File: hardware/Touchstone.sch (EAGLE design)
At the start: 69 parts, among them J3 USB-MICROB, U1 NEOPIXEL_NANO_2427, U10 TSL2591, U11 915MHz, U12 MH-Z19, U13 CCS811-I2C, U14 IAQ-CORE-C, U15 VLP-450-F, U16 VLP-450-F, U2 FT231XQ-R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

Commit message: Added pullups on CCS811's signal lines
RESET AND WAKE lines pulled up by default
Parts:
- added R12, R14: 100K, Adafruit Feather 32u4 Bluefruit LE:MICROBUILDER_RESISTOR_0402MP
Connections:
- new net N$6: R12.2, U13.RESET
- net D5: now also R14.2
- net VCC: now also R12.1, R14.1
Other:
- note added: "0.57"
- note removed: "0.56b"
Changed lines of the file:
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@@
 <?xml version="1.0" encoding="utf-8"?>
 <!DOCTYPE eagle SYSTEM "eagle.dtd">
-<eagle version="8.2.2">
+<eagle version="8.3.0">
 <drawing>
 <settings>
 <setting alwaysvectorfont="no"/>
+<setting keepoldvectorfont="yes"/>
 <setting verticaltext="up"/>
 </settings>
@@
 <part name="U$4" library="0878980426" deviceset="0878980426" device=""/>
 <part name="U$5" library="0878980426" deviceset="0878980426" device=""/>
+<part name="R12" library="Adafruit Feather 32u4 Bluefruit LE" deviceset="MICROBUILDER_RESISTOR" device="_0402MP" value="100K"/>
+<part name="R14" library="Adafruit Feather 32u4 Bluefruit LE" deviceset="MICROBUILDER_RESISTOR" device="_0402MP" value="100K"/>
+<part name="SUPPLY19" library="SparkFun-Aesthetics" deviceset="VCC" device=""/>
+<part name="SUPPLY20" library="SparkFun-Aesthetics" deviceset="VCC" device=""/>
 </parts>
 <sheets>
@@
 <text x="88.9" y="55.88" size="1.778" layer="97">0x5A</text>
 <text x="220.98" y="104.14" size="1.778" layer="97">0x77</text>
-<text x="257.556" y="-102.362" size="2.54" layer="94" font="vector" ratio="10">0.56b</text>
+<text x="257.556" y="-102.362" size="2.54" layer="94" font="vector" ratio="10">0.57</text>
 <text x="248.666" y="-87.122" size="2.54" layer="94" font="vector" ratio="10">github.crtlabs.org</text>
 <text x="157.48" y="101.6" size="1.778" layer="97">0x29</text>
@@
 <instance part="U$4" gate="G$1" x="259.08" y="101.6"/>
 <instance part="U$5" gate="G$1" x="289.56" y="101.6"/>
+<instance part="R12" gate="G$1" x="58.42" y="20.32" rot="R270"/>
+<instance part="R14" gate="G$1" x="109.22" y="20.32" rot="R270"/>
+<instance part="SUPPLY19" gate="G$1" x="58.42" y="25.4"/>
+<instance part="SUPPLY20" gate="G$1" x="109.22" y="25.4"/>
 </instances>
 <busses>
@@
 <pinref part="SUPPLY18" gate="G$1" pin="VCC"/>
 </segment>
+<segment>
+<pinref part="R12" gate="G$1" pin="1"/>
+<pinref part="SUPPLY19" gate="G$1" pin="VCC"/>
+</segment>
+<segment>
+<pinref part="R14" gate="G$1" pin="1"/>
+<pinref part="SUPPLY20" gate="G$1" pin="VCC"/>
+</segment>
 </net>
 <net name="SCL" class="0">
@@
 <wire x1="101.6" y1="7.62" x2="106.68" y2="7.62" width="0.1524" layer="91"/>
 <label x="101.6" y="7.62" size="1.778" layer="95"/>
+<wire x1="106.68" y1="7.62" x2="109.22" y2="7.62" width="0.1524" layer="91"/>
+<wire x1="106.68" y1="7.62" x2="106.68" y2="12.7" width="0.1524" layer="91"/>
+<junction x="106.68" y="7.62"/>
+<pinref part="R14" gate="G$1" pin="2"/>
+<wire x1="106.68" y1="12.7" x2="109.22" y2="12.7" width="0.1524" layer="91"/>
+<wire x1="109.22" y1="12.7" x2="109.22" y2="15.24" width="0.1524" layer="91"/>
 </segment>
 </net>
@@
 <wire x1="269.24" y1="55.88" x2="269.24" y2="63.5" width="0.1524" layer="91"/>
 <label x="261.62" y="55.88" size="1.778" layer="95"/>
+</segment>
+</net>
+<net name="N$6" class="0">
+<segment>
+<pinref part="U13" gate="G$1" pin="RESET"/>
+<pinref part="R12" gate="G$1" pin="2"/>
+<wire x1="66.04" y1="12.7" x2="58.42" y2="12.7" width="0.1524" layer="91"/>
+<wire x1="58.42" y1="12.7" x2="58.42" y2="15.24" width="0.1524" layer="91"/>
 </segment>
 </net>
@@
 </note>
 <note version="8.2" severity="warning">
-Since Version 8.2, Eagle supports online libraries. The ids
+Since Version 8.2, EAGLE supports online libraries. The ids
 of those online libraries will not be understood (or retained)
 with this version.

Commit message: Added SMD pads for T/RH breakout
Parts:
- added U$6: CONN_HDR_1.27MM_SMD_4POS, CONN_HDR_1.27MM_SMD_4POS:CONN_HDR_1.27MM_SMD_4POS
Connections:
- net GND: now also U$6.P$4
- net SCL: now also U$6.P$2
- net SDA: now also U$6.P$3
- net VCC: now also U$6.P$1
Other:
- note added: "T/RH Headers"
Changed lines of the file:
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@@
 <part name="SUPPLY1" library="SparkFun-Aesthetics" deviceset="VCC" device=""/>
 <part name="SUPPLY7" library="SparkFun-Aesthetics" deviceset="VCC" device=""/>
-<part name="U8" library="linear" library_urn="urn:adsk.eagle:library:262" deviceset="MCP1703" device="CB">
+<part name="U8" library="linear" library_urn="urn:adsk.eagle:library:262" deviceset="MCP1703" device="CB" package3d_urn="urn:adsk.eagle:package:16489/1">
 <attribute name="MF" value=""/>
 <attribute name="MPN" value="MCP1703T-2502E/CB"/>
@@
 <part name="SUPPLY19" library="SparkFun-Aesthetics" deviceset="VCC" device=""/>
 <part name="SUPPLY20" library="SparkFun-Aesthetics" deviceset="VCC" device=""/>
+<part name="U$6" library="CONN_HDR_1.27MM_SMD_4POS" deviceset="CONN_HDR_1.27MM_SMD_4POS" device=""/>
 </parts>
 <sheets>
@@
 <text x="157.48" y="101.6" size="1.778" layer="97">0x29</text>
 <text x="139.7" y="78.74" size="2.54" layer="94" font="vector">RGB LED</text>
-<text x="127" y="30.48" size="2.54" layer="94" font="vector">I2C Headers</text>
+<text x="124.46" y="30.48" size="2.54" layer="94" font="vector">I2C Headers</text>
 <text x="73.66" y="129.54" size="2.54" layer="94" font="vector">PM2.5 sensor</text>
 <text x="185.42" y="81.28" size="2.54" layer="94" font="vector">RFM69HCW</text>
@@
 <wire x1="180.34" y1="43.18" x2="180.34" y2="-12.7" width="0.1524" layer="94" style="longdash"/>
 <wire x1="116.84" y1="43.18" x2="180.34" y2="43.18" width="0.1524" layer="94" style="longdash"/>
-<text x="127" y="-5.08" size="2.54" layer="94" font="vector">5V Power</text>
+<text x="124.46" y="-5.08" size="2.54" layer="94" font="vector">5V Power</text>
 <wire x1="180.34" y1="43.18" x2="312.42" y2="43.18" width="0.1524" layer="94" style="longdash"/>
 <text x="91.44" y="-2.54" size="1.778" layer="97">0x5B</text>
 <text x="30.48" y="104.14" size="1.778" layer="97">0x40</text>
+<text x="124.46" y="12.7" size="2.54" layer="94" font="vector">T/RH Headers</text>
 </plain>
 <instances>
@@
 <instance part="SUPPLY19" gate="G$1" x="58.42" y="25.4"/>
 <instance part="SUPPLY20" gate="G$1" x="109.22" y="25.4"/>
+<instance part="U$6" gate="G$1" x="157.48" y="10.16"/>
 </instances>
 <busses>
@@
 <label x="274.32" y="99.06" size="1.778" layer="95"/>
 </segment>
+<segment>
+<pinref part="U$6" gate="G$1" pin="P$4"/>
+<wire x1="167.64" y1="10.16" x2="170.18" y2="10.16" width="0.1524" layer="91"/>
+<label x="170.18" y="10.16" size="1.778" layer="95"/>
+</segment>
 </net>
 <net name="VCC" class="0">
@@
 <pinref part="SUPPLY20" gate="G$1" pin="VCC"/>
 </segment>
+<segment>
+<pinref part="U$6" gate="G$1" pin="P$1"/>
+<wire x1="167.64" y1="17.78" x2="170.18" y2="17.78" width="0.1524" layer="91"/>
+<label x="170.18" y="17.78" size="1.778" layer="95"/>
+</segment>
 </net>
 <net name="SCL" class="0">
@@
 <label x="101.6" y="15.24" size="1.778" layer="95"/>
 </segment>
+<segment>
+<pinref part="U$6" gate="G$1" pin="P$2"/>
+<wire x1="167.64" y1="15.24" x2="170.18" y2="15.24" width="0.1524" layer="91"/>
+<label x="170.18" y="15.24" size="1.778" layer="95"/>
+</segment>
 </net>
 <net name="SDA" class="0">
@@
 <wire x1="101.6" y1="12.7" x2="104.14" y2="12.7" width="0.1524" layer="91"/>
 <label x="101.6" y="12.7" size="1.778" layer="95"/>
+</segment>
+<segment>
+<pinref part="U$6" gate="G$1" pin="P$3"/>
+<wire x1="167.64" y1="12.7" x2="170.18" y2="12.7" width="0.1524" layer="91"/>
+<label x="170.18" y="12.7" size="1.778" layer="95"/>
 </segment>
 </net>
@@
 with this version.
 </note>
+<note version="8.3" severity="warning">
+Since Version 8.3, EAGLE supports URNs for individual library
+assets (packages, symbols, and devices). The URNs of those assets
+will not be understood (or retained) with this version.
+</note>
+<note version="8.3" severity="warning">
+Since Version 8.3, EAGLE supports the association of 3D packages
+with devices in libraries, schematics, and board files. Those 3D
+packages will not be understood (or retained) with this version.
+</note>
 </compatibility>

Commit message: Version number change; minor adjustments
- Changed version number to 0.5.7 (new versioning format)
- silkscreen adjustments
- some schematic rearrangements
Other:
- note added: "0.5.7"
- note removed: "0.57"
- moved on the sheet: C18, C2, C3, J1, J2, JP1, R12, R14, R4, R7, R9, U1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

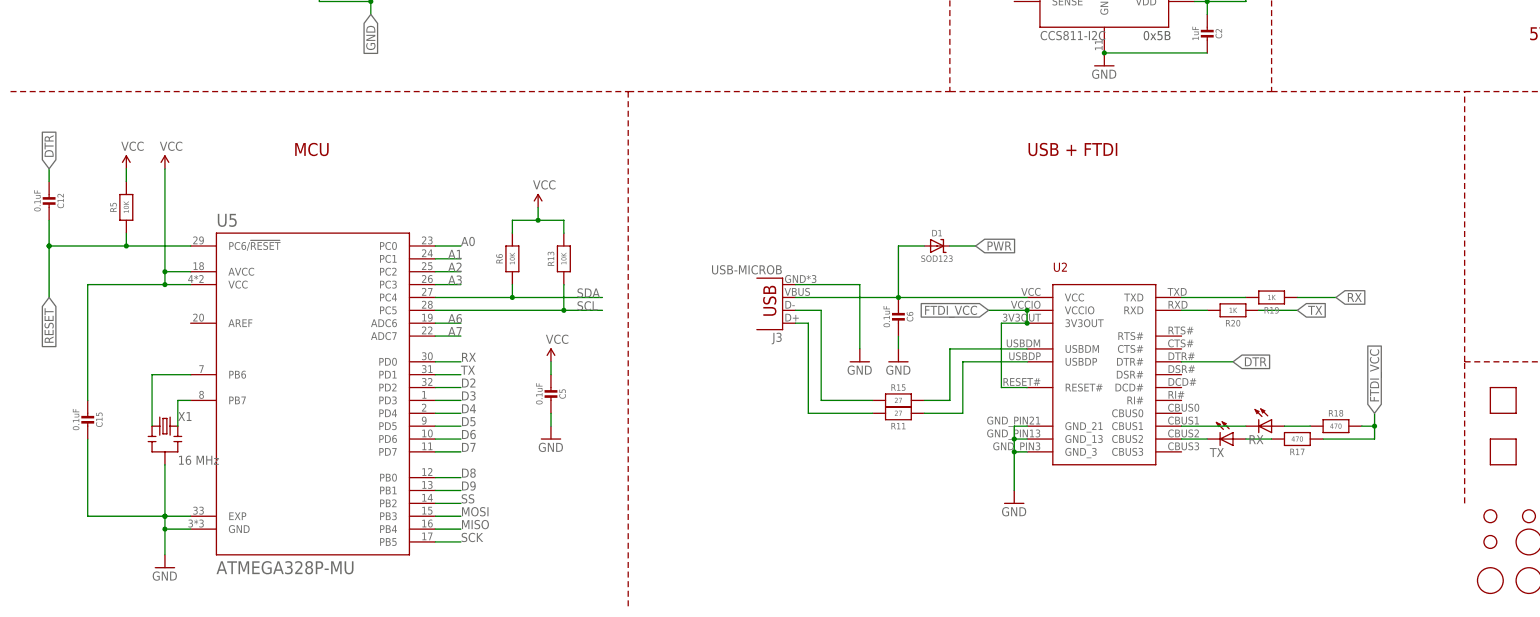
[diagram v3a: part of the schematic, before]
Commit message: Added reset button
- added momentary tactile button for resetting device (reconfiguring,
not power cycle)
- added other circuitry for button
- moved I2C headers to make space for reset button
- several traces redone to accomodate button
- minor silkscreen adjustment
- DRC/ERC checked
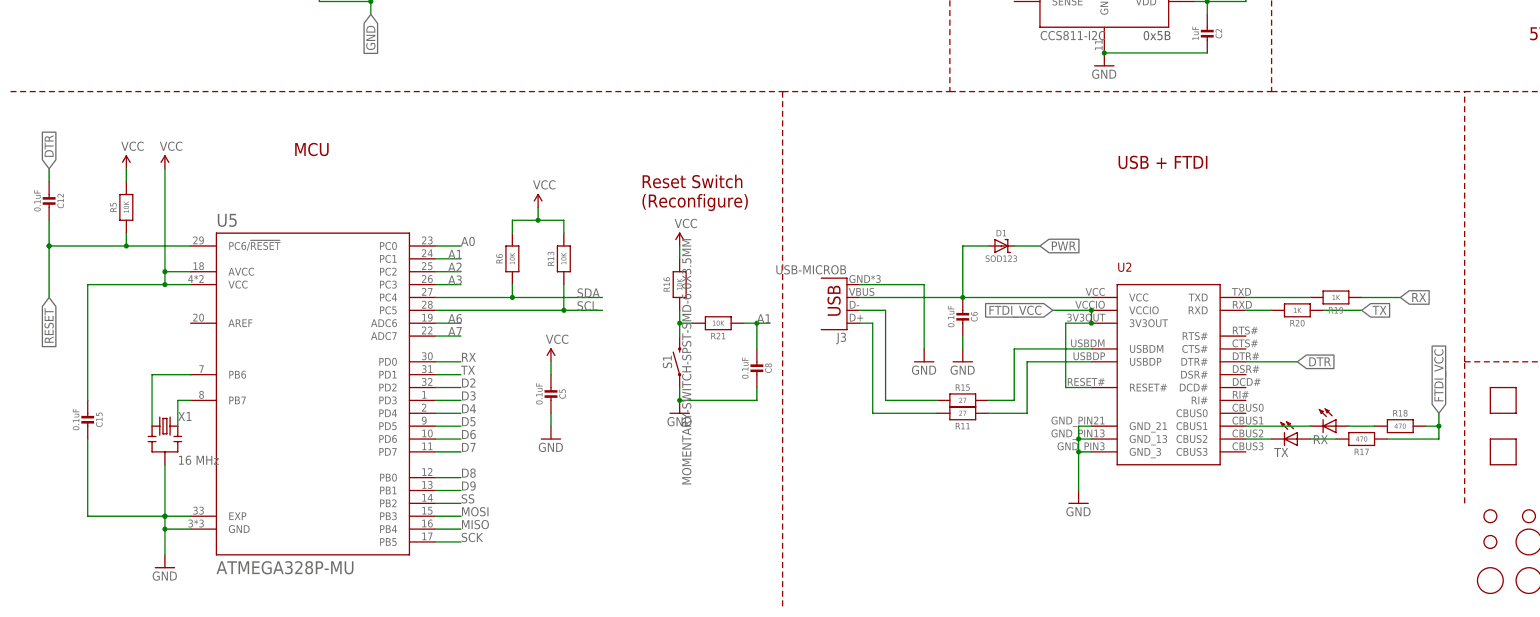
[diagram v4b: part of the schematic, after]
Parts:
- added C8: 0.1uF, Adafruit Feather 32u4 Bluefruit LE:MICROBUILDER_CAP_CERAMIC_0402MP
- added R16, R21: 10K, Adafruit Feather 32u4 Bluefruit LE:MICROBUILDER_RESISTOR_0402MP
- added S1: MOMENTARY-SWITCH-SPST-SMD-6.0X3.5MM, SparkFun-Switches:MOMENTARY-SWITCH-SPST-SMD-6.0X3.5MM
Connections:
- new net N$7: R16.1, R21.2, S1.2
- net A1: now also C8.2, R21.1
- net GND: now also C8.1, S1.1
- net VCC: now also R16.2
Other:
- note added: "Reset Switch (Reconfigure)"
- moved on the sheet: C6, D1, J3, R11, R15, R17, R18, R19, R20, RX, TX, U2

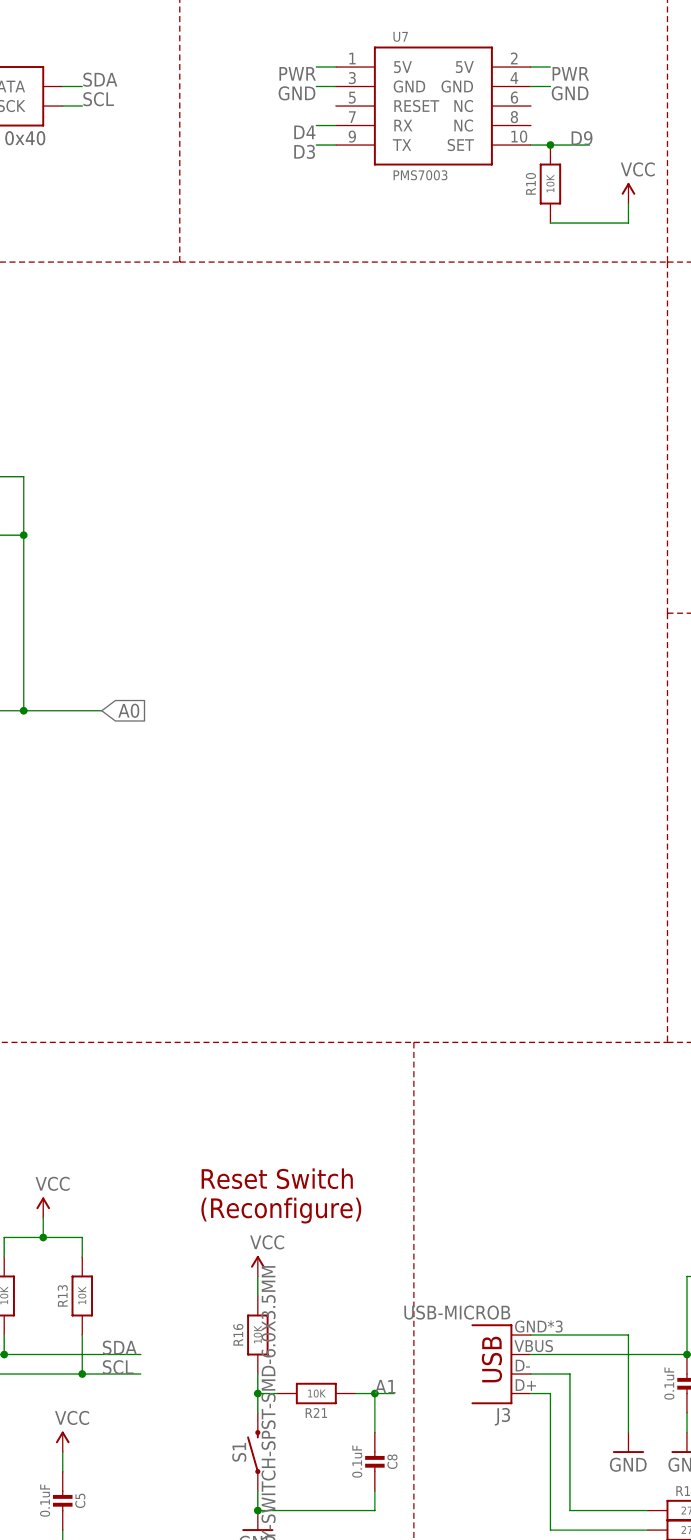
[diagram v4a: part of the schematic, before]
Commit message: Several routing adjustments
- PMS7003 TX rewired from D3 to A1 (D3 is INT pin)
- Button reqired from A1 to D3 (same reason above)
- adjusted several traces to account for the above rewiring
- Added several GND vias under MCU and FTDI (heatsink - may help a tiny
bit)
- minor silkscreen adjustments to account for above
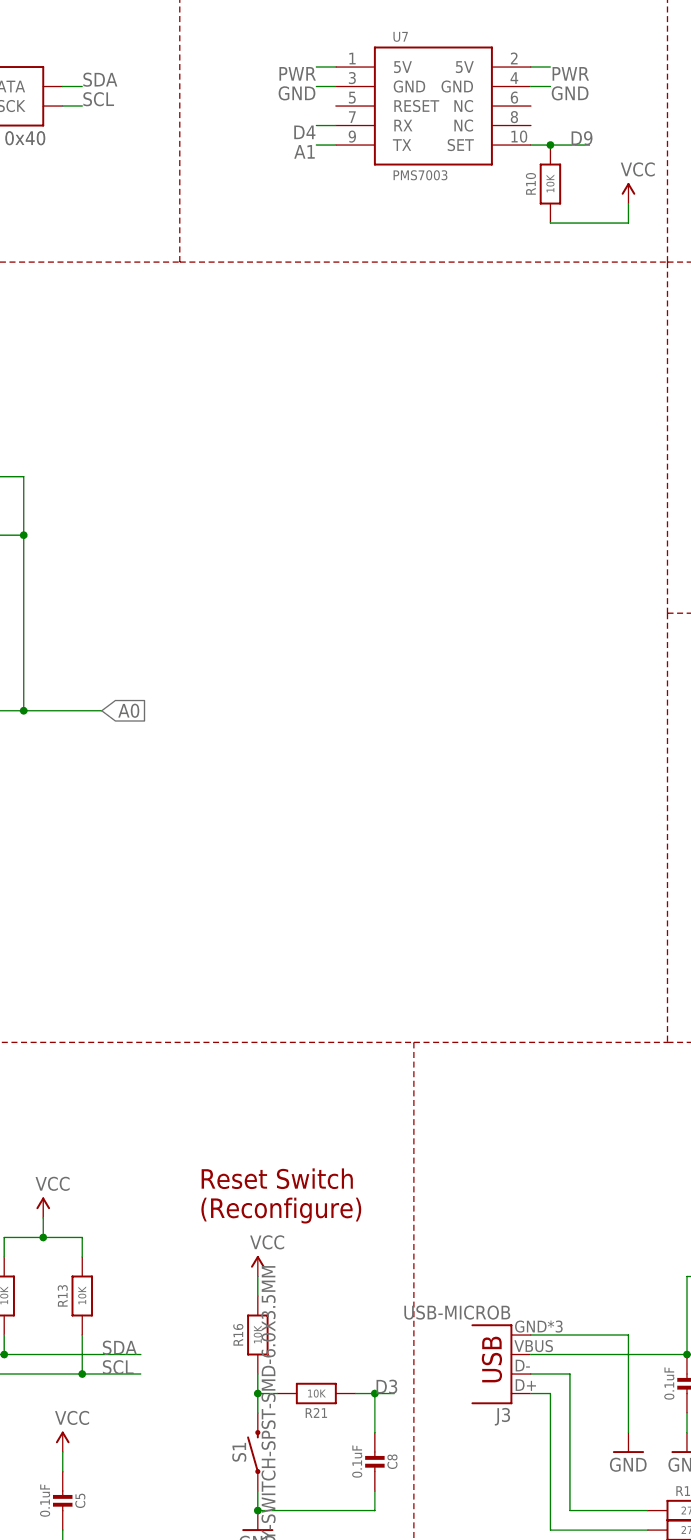
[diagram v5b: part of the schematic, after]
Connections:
- net A1: now also U7.TX; no longer C8.2, R21.1
- net D3: now also C8.2, R21.1; no longer U7.TX
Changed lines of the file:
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@@
 </segment>
 <segment>
-<pinref part="U7" gate="G$1" pin="TX"/>
-<wire x1="73.66" y1="104.14" x2="71.12" y2="104.14" width="0.1524" layer="91"/>
-<label x="71.12" y="104.14" size="1.778" layer="95" rot="R180"/>
+<pinref part="C8" gate="G$1" pin="2"/>
+<pinref part="R21" gate="G$1" pin="1"/>
+<wire x1="78.74" y1="-63.5" x2="78.74" y2="-58.42" width="0.1524" layer="91"/>
+<wire x1="78.74" y1="-58.42" x2="76.2" y2="-58.42" width="0.1524" layer="91"/>
+<wire x1="78.74" y1="-58.42" x2="81.28" y2="-58.42" width="0.1524" layer="91"/>
+<junction x="78.74" y="-58.42"/>
+<label x="78.74" y="-58.42" size="1.778" layer="95"/>
 </segment>
 </net>
@@
 </segment>
 <segment>
-<pinref part="C8" gate="G$1" pin="2"/>
-<pinref part="R21" gate="G$1" pin="1"/>
-<wire x1="78.74" y1="-63.5" x2="78.74" y2="-58.42" width="0.1524" layer="91"/>
-<wire x1="78.74" y1="-58.42" x2="76.2" y2="-58.42" width="0.1524" layer="91"/>
-<wire x1="78.74" y1="-58.42" x2="81.28" y2="-58.42" width="0.1524" layer="91"/>
-<junction x="78.74" y="-58.42"/>
-<label x="78.74" y="-58.42" size="1.778" layer="95"/>
+<pinref part="U7" gate="G$1" pin="TX"/>
+<wire x1="73.66" y1="104.14" x2="71.12" y2="104.14" width="0.1524" layer="91"/>
+<label x="71.12" y="104.14" size="1.778" layer="95" rot="R180"/>
 </segment>
 </net>
